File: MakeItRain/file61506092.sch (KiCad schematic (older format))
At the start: 5 parts, among them Q2 IRF510, Q3 2N7000

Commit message: wip for layout
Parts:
- removed Q2: IRF510, SamacSys_Parts:TO254P465X1024X2050-3P, symbol SamacSys_Parts:IRF510
- removed R3: 1M, Resistor_THT:R_Axial_DIN0207_L6.3mm_D2.5mm_P2.54mm_Vertical, symbol Device:R
- added D2: 1N53xxB, Diode_THT:D_DO-201_P15.24mm_Horizontal, symbol Diode:1N53xxB
- added D3: STPS3150RL, Diode_THT:D_DO-201_P15.24mm_Horizontal, symbol Device:D_Schottky
- added Q3: 2N7000, Package_TO_SOT_THT:TO-92_Inline, symbol Transistor_FET:2N7000
- added Q4: IRF9Z34NPBF, SamacSys_Parts:TO254P469X1042X1967-3P, symbol SamacSys_Parts:IRF9Z34NPBF
- added R10: 100k, Resistor_THT:R_Axial_DIN0207_L6.3mm_D2.5mm_P2.54mm_Vertical, symbol Device:R
- added R11: 10k, Resistor_THT:R_Axial_DIN0207_L6.3mm_D2.5mm_P2.54mm_Vertical, symbol Device:R
- added R9: 1M, Resistor_THT:R_Axial_DIN0207_L6.3mm_D2.5mm_P2.54mm_Vertical, symbol Device:R
- renumbered Q3 to Q2, R2 to R7, R4 to R8
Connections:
- net GND: now also D3.2 (A), Q3.1 (S), R9.2
- net ZoneOutputTTL: now also Q3.2 (G), R9.1
- new net: Q3.3 (D), R11.2
- new net: D2.2 (A), Q4.1, R10.2, R11.1
- new net +VDC: D2.1 (K), Q4.3, R10.1
- new net ZoneOutput: D3.1 (K), Q4.2
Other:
- moved on the sheet: Q11, R22, R23

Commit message: Routing Done need to add some more documentation to the board via silkscreen.
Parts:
- removed D2: 1N53xxB, Diode_THT:D_DO-201_P15.24mm_Horizontal, symbol Diode:1N53xxB
- added Z7: BZX79C10, DIOAD1068W53L380D172, symbol SamacSys_Parts:BZX79C10
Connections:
- net +VDC: now also Z7.1
- net at Q4.1, R10.2, R11.1: now also Z7.2
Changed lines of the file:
@@
 AR Path="/6158BC32/6152D106" Ref="Q?"  Part="1"
 AR Path="/6158BCC0/6152D106" Ref="Q?"  Part="1"
-F 0 "Q11" H 2554 3046 50  0000 L CNN
+F 0 "Q2" H 2554 3046 50  0000 L CNN
 F 1 "2N7000" H 2554 2955 50  0000 L CNN
 F 2 "Package_TO_SOT_THT:TO-92_Inline" H 2550 2925 50  0001 L CIN
@@
 AR Path="/6158BC32/6152D10C" Ref="R?"  Part="1"
 AR Path="/6158BCC0/6152D10C" Ref="R?"  Part="1"
-F 0 "R22" H 2220 3546 50  0000 L CNN
+F 0 "R7" H 2220 3546 50  0000 L CNN
 F 1 "1M" H 2220 3455 50  0000 L CNN
 F 2 "Resistor_THT:R_Axial_DIN0207_L6.3mm_D2.5mm_P2.54mm_Vertical" V 2080 3500 50  0001 C CNN
@@
 AR Path="/6158BC32/6152D112" Ref="#PWR?"  Part="1"
 AR Path="/6158BCC0/6152D112" Ref="#PWR?"  Part="1"
-F 0 "#PWR040" H 2450 3550 50  0001 C CNN
+F 0 "#PWR028" H 2450 3550 50  0001 C CNN
 F 1 "GND" H 2455 3627 50  0000 C CNN
 F 2 "" H 2450 3800 50  0001 C CNN
@@
 AR Path="/6158BC32/6152D11A" Ref="R?"  Part="1"
 AR Path="/6158BCC0/6152D11A" Ref="R?"  Part="1"
-F 0 "R23" H 2520 3546 50  0000 L CNN
+F 0 "R8" H 2520 3546 50  0000 L CNN
 F 1 "1M" H 2520 3455 50  0000 L CNN
 F 2 "Resistor_THT:R_Axial_DIN0207_L6.3mm_D2.5mm_P2.54mm_Vertical" V 2380 3500 50  0001 C CNN
@@
 AR Path="/6158BC32/6152D123" Ref="#PWR?"  Part="1"
 AR Path="/6158BCC0/6152D123" Ref="#PWR?"  Part="1"
-F 0 "#PWR039" H 2450 2450 50  0001 C CNN
+F 0 "#PWR027" H 2450 2450 50  0001 C CNN
 F 1 "+3.3V" H 2465 2773 50  0000 C CNN
 F 2 "" H 2450 2600 50  0001 C CNN
@@
 AR Path="/6158BC32/6155430A" Ref="Q?"  Part="1"
 AR Path="/6158BCC0/6155430A" Ref="Q?"  Part="1"
-F 0 "Q12" H 5954 3696 50  0000 L CNN
+F 0 "Q3" H 5954 3696 50  0000 L CNN
 F 1 "2N7000" H 5954 3605 50  0000 L CNN
 F 2 "Package_TO_SOT_THT:TO-92_Inline" H 5950 3575 50  0001 L CIN
@@
 AR Path="/6158BC32/61554310" Ref="R?"  Part="1"
 AR Path="/6158BCC0/61554310" Ref="R?"  Part="1"
-F 0 "R24" H 5620 4196 50  0000 L CNN
+F 0 "R9" H 5620 4196 50  0000 L CNN
 F 1 "1M" H 5620 4105 50  0000 L CNN
 F 2 "Resistor_THT:R_Axial_DIN0207_L6.3mm_D2.5mm_P2.54mm_Vertical" V 5480 4150 50  0001 C CNN
@@
 AR Path="/6158BC32/61554316" Ref="#PWR?"  Part="1"
 AR Path="/6158BCC0/61554316" Ref="#PWR?"  Part="1"
-F 0 "#PWR041" H 5850 4200 50  0001 C CNN
+F 0 "#PWR029" H 5850 4200 50  0001 C CNN
 F 1 "GND" H 5855 4277 50  0000 C CNN
 F 2 "" H 5850 4450 50  0001 C CNN
@@
 AR Path="/6158BC32/61554F46" Ref="R?"  Part="1"
 AR Path="/6158BCC0/61554F46" Ref="R?"  Part="1"
-F 0 "R26" H 5920 3146 50  0000 L CNN
+F 0 "R11" H 5920 3146 50  0000 L CNN
 F 1 "10k" H 5920 3055 50  0000 L CNN
 F 2 "Resistor_THT:R_Axial_DIN0207_L6.3mm_D2.5mm_P2.54mm_Vertical" V 5780 3100 50  0001 C CNN
@@
 AR Path="/6158BC32/61555474" Ref="R?"  Part="1"
 AR Path="/6158BCC0/61555474" Ref="R?"  Part="1"
-F 0 "R25" H 5920 2646 50  0000 L CNN
+F 0 "R10" H 5920 2646 50  0000 L CNN
 F 1 "100k" H 5920 2555 50  0000 L CNN
 F 2 "Resistor_THT:R_Axial_DIN0207_L6.3mm_D2.5mm_P2.54mm_Vertical" V 5780 2600 50  0001 C CNN
@@
 AR Path="/6158BCC0/615557CE" Ref="Q?"  Part="1"
 AR Path="/6158B83D/615557CE" Ref="Q13"  Part="1"
-F 0 "Q13" H 6780 2996 50  0000 L CNN
+F 0 "Q4" H 6780 2996 50  0000 L CNN
 F 1 "IRF9Z34NPBF" H 6780 2905 50  0000 L CNN
 F 2 "SamacSys_Parts:TO254P469X1042X1967-3P" H 6800 2800 50  0001 L CNN
@@
 Wire Wire Line
 	5850 2950 5850 2850
-Wire Wire Line
-	6350 2850 6250 2850
 Connection ~ 5850 2850
 Wire Wire Line
@@
 AR Path="/6158BCC0/6155EF75" Ref="#PWR?"  Part="1"
 AR Path="/6158B83D/6155EF75" Ref="#PWR042"  Part="1"
-F 0 "#PWR042" H 6250 1600 50  0001 C CNN
+F 0 "#PWR030" H 6250 1600 50  0001 C CNN
 F 1 "+VDC" H 6250 1975 50  0000 C CNN
 F 2 "" H 6250 1700 50  0001 C CNN
@@
 	1    0    0    -1
 $EndComp
-$Comp
-L Diode:1N53xxB D2
-U 1 1 615D648C
-P 6250 2300
-AR Path="/61506093/615D648C" Ref="D2"  Part="1"
-AR Path="/6158B349/615D648C" Ref="D4"  Part="1"
-AR Path="/6158B957/615D648C" Ref="D6"  Part="1"
-AR Path="/6158BA21/615D648C" Ref="D?"  Part="1"
-AR Path="/6158BA91/615D648C" Ref="D?"  Part="1"
-AR Path="/6158BC32/615D648C" Ref="D?"  Part="1"
-AR Path="/6158BCC0/615D648C" Ref="D?"  Part="1"
-AR Path="/6158B83D/615D648C" Ref="D8"  Part="1"
-F 0 "D8" V 6204 2220 50  0000 R CNN
-F 1 "1N53xxB" V 6295 2220 50  0000 R CNN
-F 2 "Diode_THT:D_DO-201_P15.24mm_Horizontal" H 6250 2125 50  0001 C CNN
-F 3 "https://diotec.com/tl_files/diotec/files/pdf/datasheets/1n5345b.pdf" H 6250 2300 50  0001 C CNN
-	1    6250 2300
-	0    -1   1    0
-$EndComp
-Wire Wire Line
-	6250 2150 6250 1700
 Connection ~ 6250 1700
 Wire Wire Line
 	6250 1700 5850 1700
-Wire Wire Line
-	6250 2450 6250 2850
-Connection ~ 6250 2850
-Wire Wire Line
-	6250 2850 5850 2850
 Wire Wire Line
 	6500 3650 6500 4300
@@
 AR Path="/6158BCC0/615DBDB1" Ref="D?"  Part="1"
 AR Path="/6158B83D/615DBDB1" Ref="D9"  Part="1"
-F 0 "D9" V 6454 3580 50  0000 L CNN
+F 0 "D3" V 6454 3580 50  0000 L CNN
 F 1 "STPS3150RL" V 6545 3580 50  0000 L CNN
 F 2 "Diode_THT:D_DO-201_P15.24mm_Horizontal" H 6500 3500 50  0001 C CNN
@@
 Wire Wire Line
 	6650 2450 6650 1700
+$Comp
+L SamacSys_Parts:BZX79C10 Z7
+U 1 1 6192AFD8
+P 6250 1950
+AR Path="/6158B957/6192AFD8" Ref="Z7"  Part="1"
+AR Path="/61506093/6192AFD8" Ref="Z5"  Part="1"
+AR Path="/6158B349/6192AFD8" Ref="Z6"  Part="1"
+AR Path="/6158B83D/6192AFD8" Ref="Z8"  Part="1"
+F 0 "Z5" V 6504 1820 50  0000 R CNN
+F 1 "BZX79C10" V 6595 1820 50  0000 R CNN
+F 2 "DIOAD1068W53L380D172" H 6650 2100 50  0001 L CNN
+F 3 "https://www.fairchildsemi.com/datasheets/BZ/BZX79C10.pdf" H 6650 2000 50  0001 L CNN
+F 4 "BZX79C10, Zener Diode, 10V +/-5 500 mW 0.2A, 2-Pin DO-35" H 6650 1900 50  0001 L CNN "Description"
+F 5 "" H 6650 1800 50  0001 L CNN "Height"
+F 6 "512-BZX79C10" H 6650 1700 50  0001 L CNN "Mouser Part Number"
+F 7 "https://www.mouser.co.uk/ProductDetail/ON-Semiconductor-Fairchild/BZX79C10?qs=FITO%2F%2FQgYDkGEXVpK3DyhQ%3D%3D" H 6650 1600 50  0001 L CNN "Mouser Price/Stock"
+F 8 "ON Semiconductor" H 6650 1500 50  0001 L CNN "Manufacturer_Name"
+F 9 "BZX79C10" H 6650 1400 50  0001 L CNN "Manufacturer_Part_Number"
+	1    6250 1950
+	0    -1   1    0
+$EndComp
+Wire Wire Line
+	5850 2850 6250 2850
+Wire Wire Line
+	6250 1950 6250 1700
+Wire Wire Line
+	6250 2550 6250 2850
+Connection ~ 6250 2850
+Wire Wire Line
+	6250 2850 6350 2850
 $EndSCHEMATC

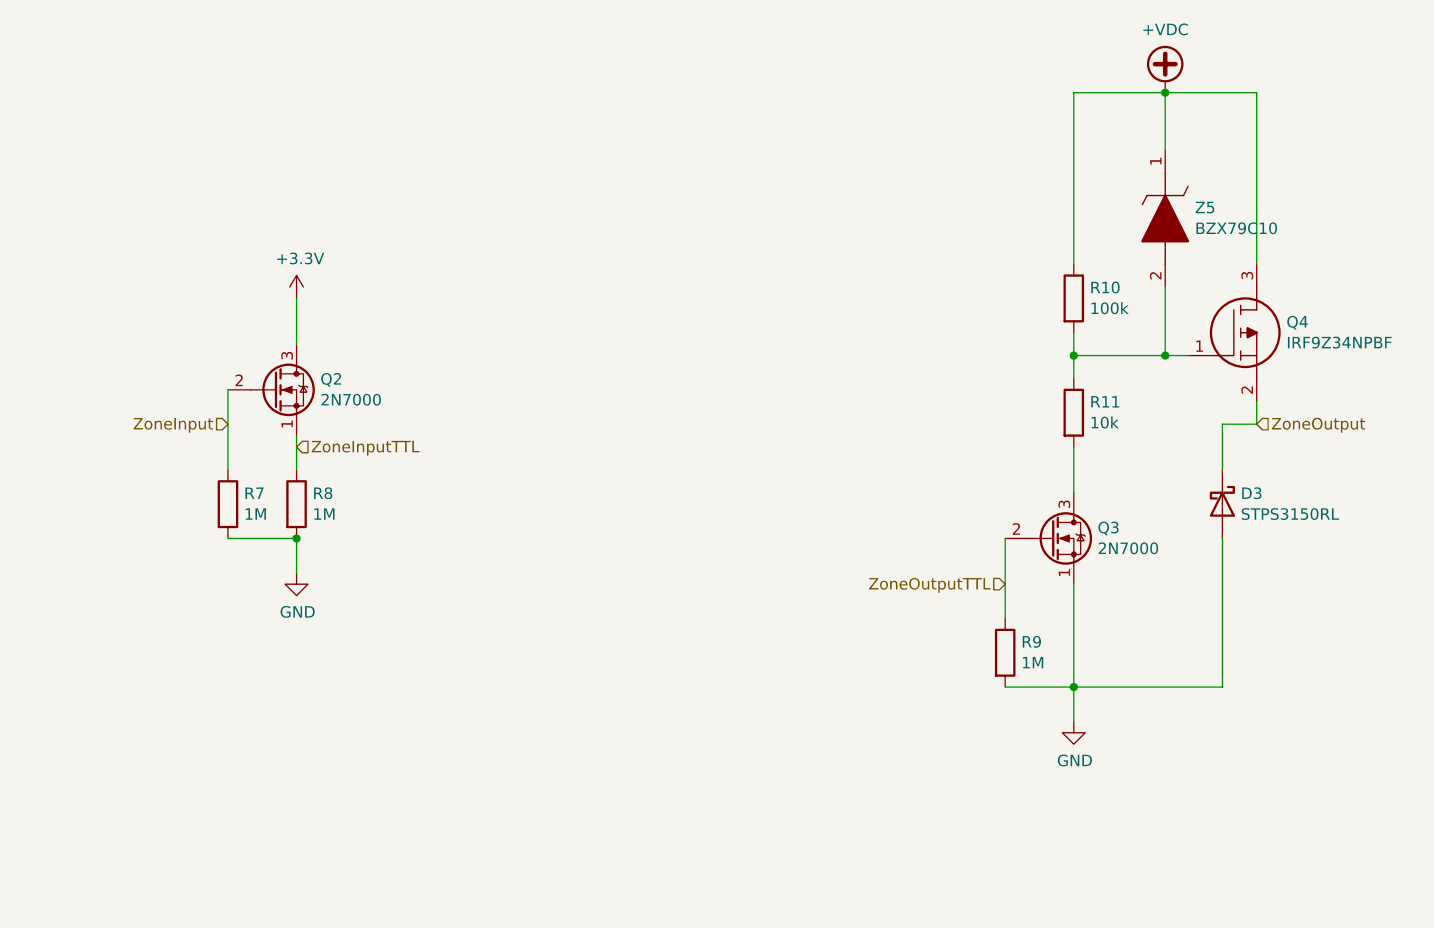
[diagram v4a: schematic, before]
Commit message: adding the debounce caps haven't moved some stuff around on the board to fit these in.
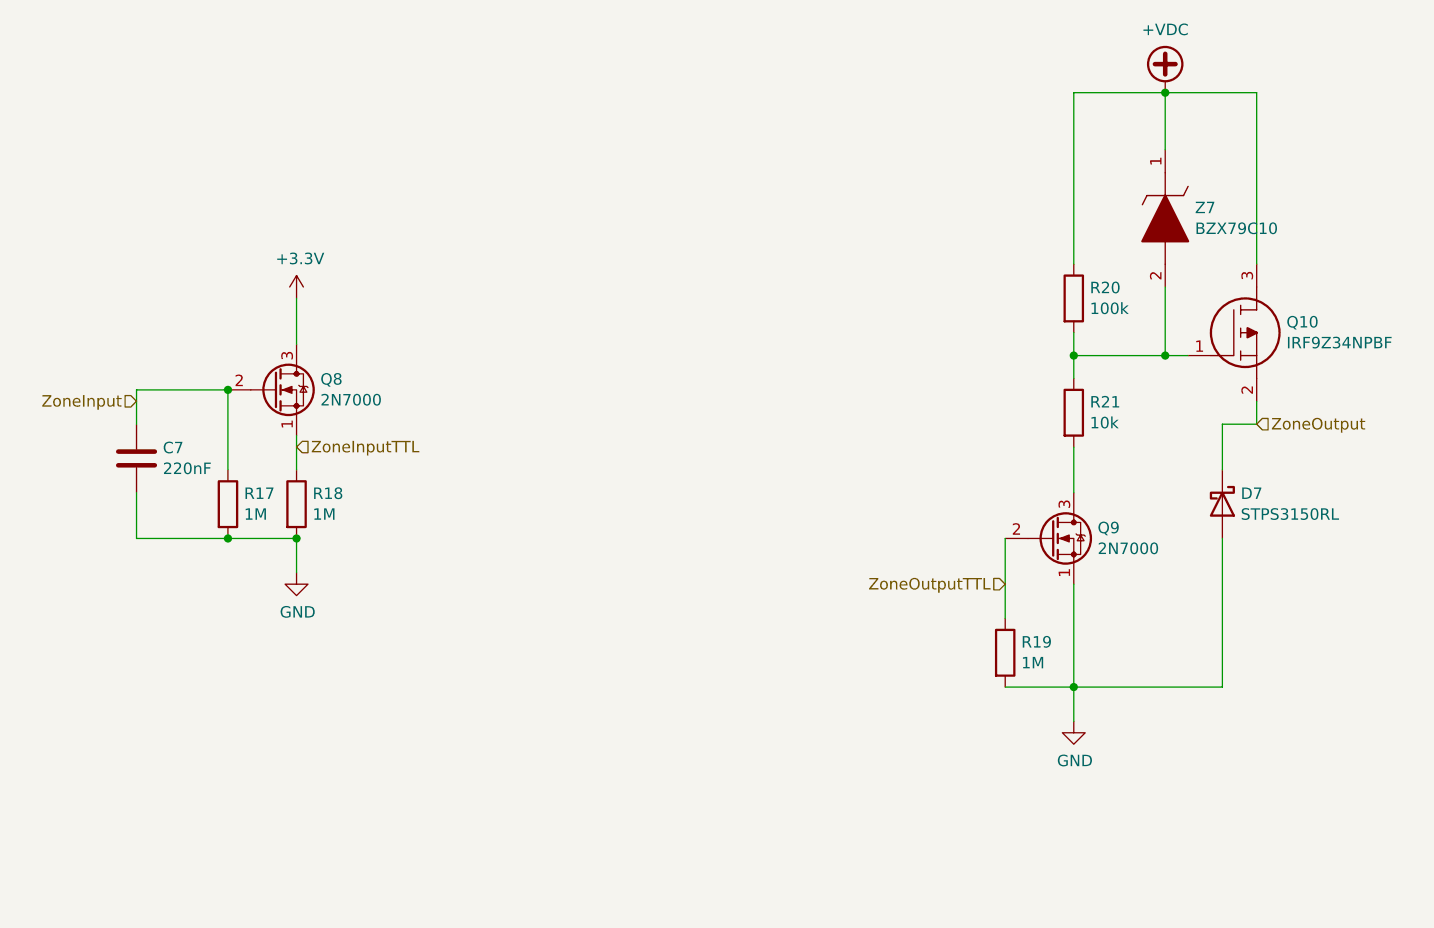
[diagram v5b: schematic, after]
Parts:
- added C5: 220nF, Capacitor_THT:C_Disc_D5.1mm_W3.2mm_P5.00mm, symbol Device:C
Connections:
- net GND: now also C5.2
- net ZoneInput: now also C5.1
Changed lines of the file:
@@
 $Descr A4 11693 8268
 encoding utf-8
-Sheet 2 5
+Sheet 4 5
 Title ""
 Date ""
@@
 AR Path="/6158BC32/6152D106" Ref="Q?"  Part="1"
 AR Path="/6158BCC0/6152D106" Ref="Q?"  Part="1"
-F 0 "Q2" H 2554 3046 50  0000 L CNN
+F 0 "Q8" H 2554 3046 50  0000 L CNN
 F 1 "2N7000" H 2554 2955 50  0000 L CNN
 F 2 "Package_TO_SOT_THT:TO-92_Inline" H 2550 2925 50  0001 L CIN
@@
 AR Path="/6158BC32/6152D10C" Ref="R?"  Part="1"
 AR Path="/6158BCC0/6152D10C" Ref="R?"  Part="1"
-F 0 "R7" H 2220 3546 50  0000 L CNN
+F 0 "R17" H 2220 3546 50  0000 L CNN
 F 1 "1M" H 2220 3455 50  0000 L CNN
 F 2 "Resistor_THT:R_Axial_DIN0207_L6.3mm_D2.5mm_P2.54mm_Vertical" V 2080 3500 50  0001 C CNN
@@
 AR Path="/6158BC32/6152D112" Ref="#PWR?"  Part="1"
 AR Path="/6158BCC0/6152D112" Ref="#PWR?"  Part="1"
-F 0 "#PWR028" H 2450 3550 50  0001 C CNN
+F 0 "#PWR036" H 2450 3550 50  0001 C CNN
 F 1 "GND" H 2455 3627 50  0000 C CNN
 F 2 "" H 2450 3800 50  0001 C CNN
@@
 Wire Wire Line
 	2450 3800 2450 3650
-Wire Wire Line
-	2150 3650 2450 3650
 $Comp
 L Device:R R?
@@
 AR Path="/6158BC32/6152D11A" Ref="R?"  Part="1"
 AR Path="/6158BCC0/6152D11A" Ref="R?"  Part="1"
-F 0 "R8" H 2520 3546 50  0000 L CNN
+F 0 "R18" H 2520 3546 50  0000 L CNN
 F 1 "1M" H 2520 3455 50  0000 L CNN
 F 2 "Resistor_THT:R_Axial_DIN0207_L6.3mm_D2.5mm_P2.54mm_Vertical" V 2380 3500 50  0001 C CNN
@@
 AR Path="/6158BC32/6152D123" Ref="#PWR?"  Part="1"
 AR Path="/6158BCC0/6152D123" Ref="#PWR?"  Part="1"
-F 0 "#PWR027" H 2450 2450 50  0001 C CNN
+F 0 "#PWR035" H 2450 2450 50  0001 C CNN
 F 1 "+3.3V" H 2465 2773 50  0000 C CNN
 F 2 "" H 2450 2600 50  0001 C CNN
@@
 Wire Wire Line
 	2450 2800 2450 2600
-Text HLabel 2150 3150 0    50   Input ~ 0
+Text HLabel 1750 3050 0    50   Input ~ 0
 ZoneInput
 Text HLabel 2450 3250 2    50   Input ~ 0
@@
 AR Path="/6158BC32/6155430A" Ref="Q?"  Part="1"
 AR Path="/6158BCC0/6155430A" Ref="Q?"  Part="1"
-F 0 "Q3" H 5954 3696 50  0000 L CNN
+F 0 "Q9" H 5954 3696 50  0000 L CNN
 F 1 "2N7000" H 5954 3605 50  0000 L CNN
 F 2 "Package_TO_SOT_THT:TO-92_Inline" H 5950 3575 50  0001 L CIN
@@
 AR Path="/6158BC32/61554310" Ref="R?"  Part="1"
 AR Path="/6158BCC0/61554310" Ref="R?"  Part="1"
-F 0 "R9" H 5620 4196 50  0000 L CNN
+F 0 "R19" H 5620 4196 50  0000 L CNN
 F 1 "1M" H 5620 4105 50  0000 L CNN
 F 2 "Resistor_THT:R_Axial_DIN0207_L6.3mm_D2.5mm_P2.54mm_Vertical" V 5480 4150 50  0001 C CNN
@@
 AR Path="/6158BC32/61554316" Ref="#PWR?"  Part="1"
 AR Path="/6158BCC0/61554316" Ref="#PWR?"  Part="1"
-F 0 "#PWR029" H 5850 4200 50  0001 C CNN
+F 0 "#PWR037" H 5850 4200 50  0001 C CNN
 F 1 "GND" H 5855 4277 50  0000 C CNN
 F 2 "" H 5850 4450 50  0001 C CNN
@@
 AR Path="/6158BC32/61554F46" Ref="R?"  Part="1"
 AR Path="/6158BCC0/61554F46" Ref="R?"  Part="1"
-F 0 "R11" H 5920 3146 50  0000 L CNN
+F 0 "R21" H 5920 3146 50  0000 L CNN
 F 1 "10k" H 5920 3055 50  0000 L CNN
 F 2 "Resistor_THT:R_Axial_DIN0207_L6.3mm_D2.5mm_P2.54mm_Vertical" V 5780 3100 50  0001 C CNN
@@
 AR Path="/6158BC32/61555474" Ref="R?"  Part="1"
 AR Path="/6158BCC0/61555474" Ref="R?"  Part="1"
-F 0 "R10" H 5920 2646 50  0000 L CNN
+F 0 "R20" H 5920 2646 50  0000 L CNN
 F 1 "100k" H 5920 2555 50  0000 L CNN
 F 2 "Resistor_THT:R_Axial_DIN0207_L6.3mm_D2.5mm_P2.54mm_Vertical" V 5780 2600 50  0001 C CNN
@@
 AR Path="/6158BCC0/615557CE" Ref="Q?"  Part="1"
 AR Path="/6158B83D/615557CE" Ref="Q13"  Part="1"
-F 0 "Q4" H 6780 2996 50  0000 L CNN
+F 0 "Q10" H 6780 2996 50  0000 L CNN
 F 1 "IRF9Z34NPBF" H 6780 2905 50  0000 L CNN
 F 2 "SamacSys_Parts:TO254P469X1042X1967-3P" H 6800 2800 50  0001 L CNN
@@
 AR Path="/6158BCC0/6155EF75" Ref="#PWR?"  Part="1"
 AR Path="/6158B83D/6155EF75" Ref="#PWR042"  Part="1"
-F 0 "#PWR030" H 6250 1600 50  0001 C CNN
+F 0 "#PWR038" H 6250 1600 50  0001 C CNN
 F 1 "+VDC" H 6250 1975 50  0000 C CNN
 F 2 "" H 6250 1700 50  0001 C CNN
@@
 AR Path="/6158BCC0/615DBDB1" Ref="D?"  Part="1"
 AR Path="/6158B83D/615DBDB1" Ref="D9"  Part="1"
-F 0 "D3" V 6454 3580 50  0000 L CNN
+F 0 "D7" V 6454 3580 50  0000 L CNN
 F 1 "STPS3150RL" V 6545 3580 50  0000 L CNN
 F 2 "Diode_THT:D_DO-201_P15.24mm_Horizontal" H 6500 3500 50  0001 C CNN
@@
 AR Path="/6158B349/6192AFD8" Ref="Z6"  Part="1"
 AR Path="/6158B83D/6192AFD8" Ref="Z8"  Part="1"
-F 0 "Z5" V 6504 1820 50  0000 R CNN
+F 0 "Z7" V 6504 1820 50  0000 R CNN
 F 1 "BZX79C10" V 6595 1820 50  0000 R CNN
 F 2 "DIOAD1068W53L380D172" H 6650 2100 50  0001 L CNN
@@
 Wire Wire Line
 	6250 2850 6350 2850
+$Comp
+L Device:C C5
+U 1 1 6194D07B
+P 1750 3300
+AR Path="/61506093/6194D07B" Ref="C5"  Part="1"
+AR Path="/6158B349/6194D07B" Ref="C6"  Part="1"
+AR Path="/6158B957/6194D07B" Ref="C7"  Part="1"
+AR Path="/6158B83D/6194D07B" Ref="C8"  Part="1"
+F 0 "C7" H 1865 3346 50  0000 L CNN
+F 1 "220nF" H 1865 3255 50  0000 L CNN
+F 2 "Capacitor_THT:C_Disc_D5.1mm_W3.2mm_P5.00mm" H 1788 3150 50  0001 C CNN
+F 3 "~" H 1750 3300 50  0001 C CNN
+	1    1750 3300
+	1    0    0    -1
+$EndComp
+Wire Wire Line
+	1750 3450 1750 3650
+Connection ~ 2150 3650
+Wire Wire Line
+	2150 3650 2450 3650
+Wire Wire Line
+	1750 3150 1750 3000
+Wire Wire Line
+	1750 3650 2150 3650
+Wire Wire Line
+	1750 3000 2150 3000
+Connection ~ 2150 3000
 $EndSCHEMATC
